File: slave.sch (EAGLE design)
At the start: 362 parts, among them J2 EB21A-06-D, J3 EB21A-06-D, J4 EB21A-06-D, J5 EB21A-06-D, J6 282837-9, J7 282837-9, J8 282837-9, J9 1715250000, Q1 DMN2056U-7, Q10 DMN2056U-7, Q11 DMN2056U-7, Q12 DMN2056U-7, Q13 DMN2056U-7, Q14 DMN2056U-7, Q15 DMN2056U-7, Q16 DMN2056U-7, Q17 DMN2056U-7, Q18 DMN2056U-7, Q19 DMN2056U-7, Q2 DMN2056U-7, Q20 DMN2056U-7, Q21 DMN2056U-7, Q22 DMN2056U-7, Q23 DMN2056U-7, Q24 DMN2056U-7, Q25 DMN2056U-7, Q26 DMN2056U-7, Q27 DMN2056U-7, Q28 DMN2056U-7, Q29 DMN2056U-7, Q3 DMN2056U-7, Q30 DMN2056U-7, Q31 DMN2056U-7, Q32 DMN2056U-7, Q33 DMN2056U-7, Q34 DMN2056U-7, Q35 DMN2056U-7, Q36 DMN2056U-7, Q37 DMN2056U-7, Q38 DMN2056U-7, Q39 DMN2056U-7, Q4 DMN2056U-7, Q40 DMN2056U-7, Q41 DMN2056U-7, Q42 DMN2056U-7, Q5 DMN2056U-7, Q7 DMN2056U-7, Q8 DMN2056U-7, Q9 DMN2056U-7, U1 INA332AIDGKR, U10 INA332AIDGKR, U11 INA332AIDGKR, U12 INA332AIDGKR, U13 INA332AIDGKR, U14 INA332AIDGKR, U15 INA332AIDGKR, U16 INA332AIDGKR, U17 INA332AIDGKR, U18 INA332AIDGKR, U19 INA332AIDGKR, U2 AP2112K-3.3TRG1, U20 INA332AIDGKR, U21 INA332AIDGKR, U22 INA332AIDGKR, U23 INA332AIDGKR, U24 INA332AIDGKR, U25 INA332AIDGKR, U26 INA332AIDGKR, U27 INA332AIDGKR, U28 INA332AIDGKR, U3 MCP23008-E/P, U4 MCP23008-E/P, U5 MCP23008-E/P, U6 MC74HCT4851ADR2G, U7 MC74HCT4851ADR2G, U8 MC74HCT4851ADR2G, U9 MC74HCT4851ADR2G

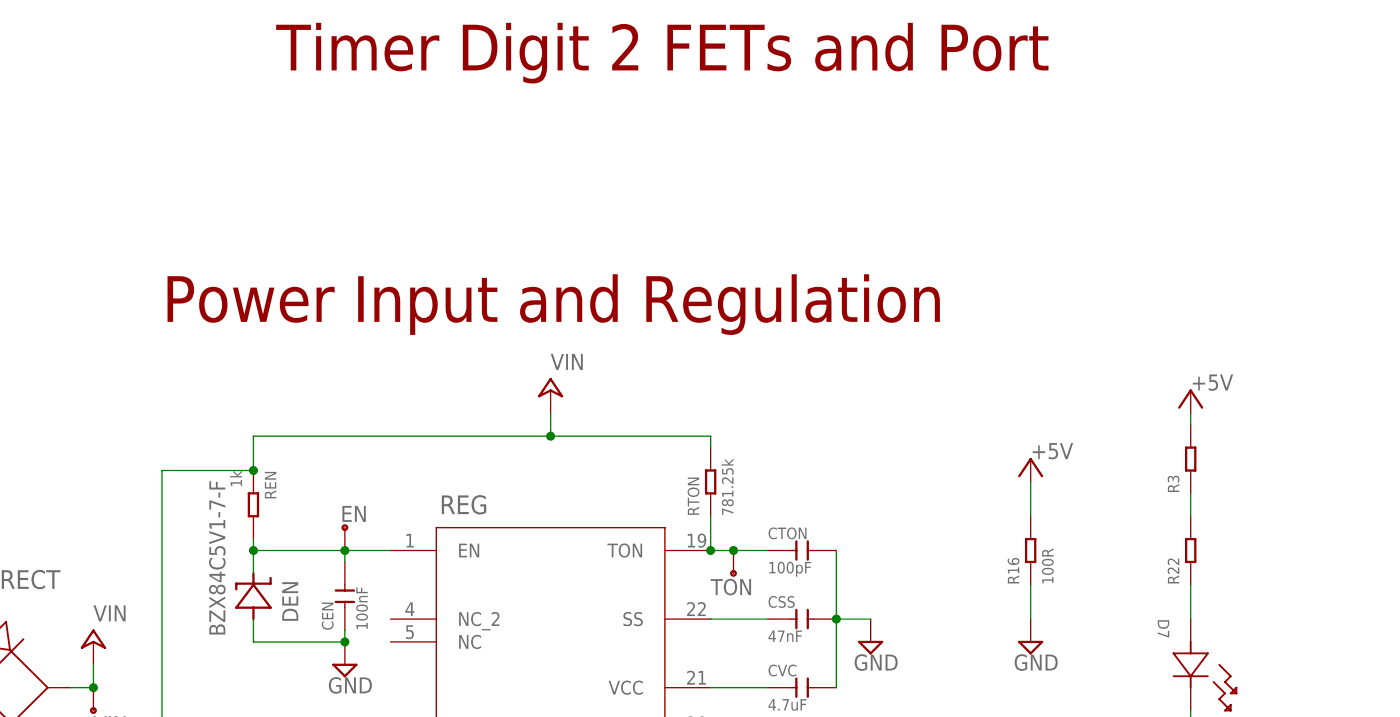
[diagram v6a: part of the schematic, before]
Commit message: updated RTON 781.25k resistor with series of 698k and 82.5k resistors, generated gerber and bom, cpl files
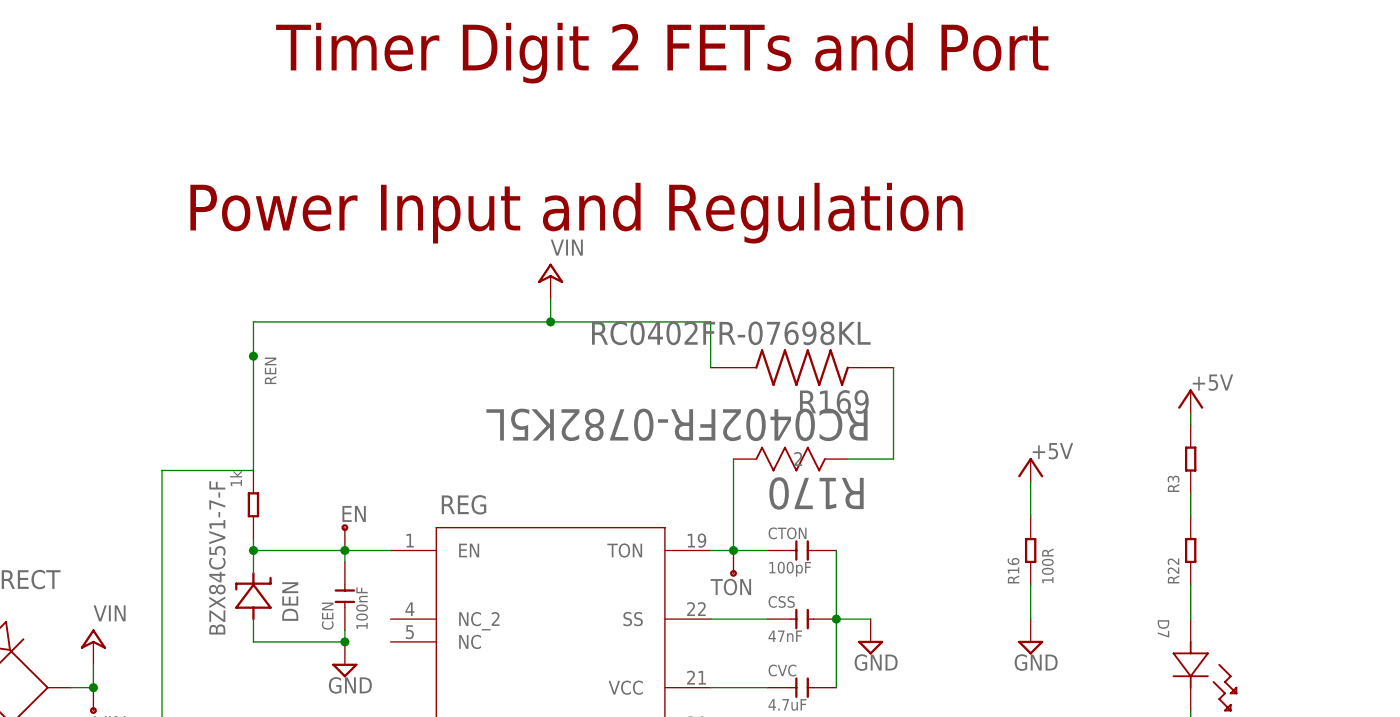
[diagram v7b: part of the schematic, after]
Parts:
- removed RTON: 781.25k, OPL_Resistor:SMD-RES-0R-1%-1/10W(0603)
- added R169: RC0402FR-07698KL, RC0402FR-07698KL:RC0402FR-07698KL
- added R170: RC0402FR-0782K5L, RC0402FR-0782K5L:RC0402FR-0782K5L
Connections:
- new net N$52: R169.1, R170.2
- net TON: now also R170.1; no longer RTON.1
- net VIN: now also R169.2; no longer RTON.2
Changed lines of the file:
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@@
 <layers>
 <layer number="1" name="Top" color="4" fill="1" visible="no" active="no"/>
-<layer number="2" name="Route2" color="21" fill="1" visible="no" active="no"/>
-<layer number="3" name="Route3" color="4" fill="3" visible="no" active="no"/>
-<layer number="4" name="Route4" color="1" fill="4" visible="no" active="no"/>
-<layer number="5" name="Route5" color="4" fill="4" visible="no" active="no"/>
-<layer number="6" name="Route6" color="1" fill="8" visible="no" active="no"/>
-<layer number="7" name="Route7" color="4" fill="8" visible="no" active="no"/>
-<layer number="8" name="Route8" color="1" fill="2" visible="no" active="no"/>
-<layer number="9" name="Route9" color="4" fill="2" visible="no" active="no"/>
-<layer number="10" name="Route10" color="1" fill="7" visible="no" active="no"/>
-<layer number="11" name="Route11" color="4" fill="7" visible="no" active="no"/>
-<layer number="12" name="Route12" color="1" fill="5" visible="no" active="no"/>
-<layer number="13" name="Route13" color="4" fill="5" visible="no" active="no"/>
-<layer number="14" name="Route14" color="1" fill="6" visible="no" active="no"/>
-<layer number="15" name="Route15" color="19" fill="1" visible="no" active="no"/>
+<layer number="2" name="Route2" color="16" fill="1" visible="no" active="no"/>
+<layer number="3" name="Route3" color="17" fill="1" visible="no" active="no"/>
+<layer number="4" name="Route4" color="18" fill="1" visible="no" active="no"/>
+<layer number="5" name="Route5" color="19" fill="1" visible="no" active="no"/>
+<layer number="6" name="Route6" color="25" fill="1" visible="no" active="no"/>
+<layer number="7" name="Route7" color="26" fill="1" visible="no" active="no"/>
+<layer number="8" name="Route8" color="27" fill="1" visible="no" active="no"/>
+<layer number="9" name="Route9" color="28" fill="1" visible="no" active="no"/>
+<layer number="10" name="Route10" color="29" fill="1" visible="no" active="no"/>
+<layer number="11" name="Route11" color="30" fill="1" visible="no" active="no"/>
+<layer number="12" name="Route12" color="20" fill="1" visible="no" active="no"/>
+<layer number="13" name="Route13" color="21" fill="1" visible="no" active="no"/>
+<layer number="14" name="Route14" color="22" fill="1" visible="no" active="no"/>
+<layer number="15" name="Route15" color="23" fill="1" visible="no" active="no"/>
 <layer number="16" name="Bottom" color="1" fill="1" visible="no" active="no"/>
 <layer number="17" name="Pads" color="2" fill="1" visible="no" active="no"/>
 <layer number="18" name="Vias" color="2" fill="1" visible="no" active="no"/>
 <layer number="19" name="Unrouted" color="6" fill="1" visible="no" active="no"/>
-<layer number="20" name="Dimension" color="15" fill="1" visible="no" active="no"/>
+<layer number="20" name="Dimension" color="24" fill="1" visible="no" active="no"/>
 <layer number="21" name="tPlace" color="7" fill="1" visible="no" active="no"/>
 <layer number="22" name="bPlace" color="7" fill="1" visible="no" active="no"/>
@@
 <part name="R1" library="OPL_Resistor" library_urn="urn:adsk.eagle:library:8004883" deviceset="SMD-RES-0R-1%-1/10W(0603)" device="" package3d_urn="urn:adsk.eagle:package:8004941/1" value="5.1k"/>
 <part name="R2" library="OPL_Resistor" library_urn="urn:adsk.eagle:library:8004883" deviceset="SMD-RES-0R-1%-1/10W(0603)" device="" package3d_urn="urn:adsk.eagle:package:8004941/1" value="27k"/>
-<part name="RTON" library="OPL_Resistor" library_urn="urn:adsk.eagle:library:8004883" deviceset="SMD-RES-0R-1%-1/10W(0603)" device="" package3d_urn="urn:adsk.eagle:package:8004941/1" value="781.25k"/>
 <part name="CSS" library="OPL_Capacitor" library_urn="urn:adsk.eagle:library:8004261" deviceset="CERAMIC-1NF-50V-10%-X7R(0603)" device="" package3d_urn="urn:adsk.eagle:package:8004287/1" value="47nF"/>
 <part name="CIN1" library="OPL_Capacitor" library_urn="urn:adsk.eagle:library:8004261" deviceset="CERAMIC-4.7UF-25V-10%-X5R(0805)" device="" package3d_urn="urn:adsk.eagle:package:8004286/1" value="10uF"/>
@@
 <part name="R168" library="RLC16-R100JTP - 100mOhm" deviceset="RLC16-R100JTP" device="" value="1m"/>
 <part name="SUPPLY37" library="supply2" library_urn="urn:adsk.eagle:library:372" deviceset="GND" device=""/>
+<part name="R169" library="RC0402FR-07698KL" deviceset="RC0402FR-07698KL" device=""/>
+<part name="R170" library="RC0402FR-0782K5L" deviceset="RC0402FR-0782K5L" device=""/>
 </parts>
 <sheets>
@@
 <plain>
 <frame x1="1270" y1="-635" x2="1955.8" y2="127" columns="8" rows="5" layer="94"/>
-<text x="1399.54" y="-469.9" size="5.08" layer="94">Power Input and Regulation</text>
+<text x="1402.08" y="-459.74" size="5.08" layer="94">Power Input and Regulation</text>
 <text x="1450.34" y="-591.82" size="5.08" layer="94" align="bottom-center">Power to ESP32
 (via 3V3 REG)</text>
@@
 <attribute name="VALUE" x="1485.9" y="-527.05" size="1.27" layer="96" ratio="10" rot="R270"/>
 </instance>
-<instance part="RTON" gate="G$1" x="1460.5" y="-487.68" smashed="yes" rot="R90">
-<attribute name="NAME" x="1459.23" y="-491.49" size="1.27" layer="95" ratio="10" rot="R90"/>
-<attribute name="VALUE" x="1463.04" y="-491.49" size="1.27" layer="96" ratio="10" rot="R90"/>
-</instance>
 <instance part="CSS" gate="G$1" x="1470.66" y="-502.92" smashed="yes">
 <attribute name="NAME" x="1466.85" y="-501.65" size="1.27" layer="95" ratio="10"/>
@@
 </instance>
 <instance part="REN" gate="G$1" x="1409.7" y="-490.22" smashed="yes" rot="R270">
-<attribute name="NAME" x="1410.97" y="-486.41" size="1.27" layer="95" ratio="10" rot="R270"/>
+<attribute name="NAME" x="1410.97" y="-473.71" size="1.27" layer="95" ratio="10" rot="R270"/>
 <attribute name="VALUE" x="1407.16" y="-486.41" size="1.27" layer="96" ratio="10" rot="R270"/>
 </instance>
@@
 <attribute name="VALUE" x="1406.5758" y="-504.8504" size="1.778" layer="96" rot="R90"/>
 </instance>
-<instance part="P+2" gate="1" x="1442.72" y="-477.52" smashed="yes">
-<attribute name="VALUE" x="1442.72" y="-475.234" size="1.778" layer="96"/>
+<instance part="P+2" gate="1" x="1442.72" y="-464.82" smashed="yes">
+<attribute name="VALUE" x="1442.72" y="-462.534" size="1.778" layer="96"/>
 </instance>
 <instance part="P+3" gate="1" x="1391.92" y="-505.46" smashed="yes">
@@
 <attribute name="VALUE" x="1826.895" y="-523.875" size="1.778" layer="96"/>
 </instance>
+<instance part="R169" gate="G$1" x="1470.66" y="-474.98" smashed="yes" rot="R180">
+<attribute name="NAME" x="1478.284440625" y="-477.52148125" size="2.54148125" layer="95" rot="R180"/>
+<attribute name="VALUE" x="1478.28996875" y="-469.893359375" size="2.54331875" layer="96" rot="R180"/>
+</instance>
+<instance part="R170" gate="A" x="1475.74" y="-485.14" smashed="yes" rot="R180">
+<attribute name="VALUE" x="1478.3562" y="-479.6028" size="3.4798" layer="96" ratio="10" rot="SR180"/>
+<attribute name="NAME" x="1477.9244" y="-487.2228" size="3.4798" layer="95" ratio="10" rot="SR180"/>
+</instance>
 </instances>
 <busses>
@@
 <segment>
 <pinref part="CTON" gate="G$1" pin="1"/>
-<pinref part="RTON" gate="G$1" pin="1"/>
 <wire x1="1460.5" y1="-495.3" x2="1463.04" y2="-495.3" width="0.1524" layer="91"/>
 <wire x1="1463.04" y1="-495.3" x2="1466.85" y2="-495.3" width="0.1524" layer="91"/>
-<wire x1="1460.5" y1="-495.3" x2="1460.5" y2="-491.49" width="0.1524" layer="91"/>
 <pinref part="REG" gate="A" pin="TON"/>
-<junction x="1460.5" y="-495.3"/>
 <pinref part="TON" gate="G$1" pin="1"/>
 <junction x="1463.04" y="-495.3"/>
+<pinref part="R170" gate="A" pin="1"/>
+<wire x1="1463.04" y1="-485.14" x2="1463.04" y2="-495.3" width="0.1524" layer="91"/>
 </segment>
 </net>
@@
 <wire x1="1399.54" y1="-486.41" x2="1399.54" y2="-519.43" width="0.1524" layer="91"/>
 <junction x="1399.54" y="-519.43"/>
-<wire x1="1409.7" y1="-486.41" x2="1409.7" y2="-482.6" width="0.1524" layer="91"/>
-<wire x1="1409.7" y1="-482.6" x2="1442.72" y2="-482.6" width="0.1524" layer="91"/>
-<junction x="1409.7" y="-486.41"/>
-<wire x1="1442.72" y1="-482.6" x2="1442.72" y2="-480.06" width="0.1524" layer="91"/>
-<pinref part="RTON" gate="G$1" pin="2"/>
-<wire x1="1442.72" y1="-482.6" x2="1460.5" y2="-482.6" width="0.1524" layer="91"/>
-<wire x1="1460.5" y1="-482.6" x2="1460.5" y2="-483.87" width="0.1524" layer="91"/>
-<junction x="1442.72" y="-482.6"/>
+<wire x1="1409.7" y1="-486.41" x2="1409.7" y2="-469.9" width="0.1524" layer="91"/>
+<wire x1="1409.7" y1="-469.9" x2="1442.72" y2="-469.9" width="0.1524" layer="91"/>
+<junction x="1409.7" y="-473.71"/>
+<wire x1="1442.72" y1="-469.9" x2="1442.72" y2="-467.36" width="0.1524" layer="91"/>
+<wire x1="1442.72" y1="-469.9" x2="1460.5" y2="-469.9" width="0.1524" layer="91"/>
+<wire x1="1460.5" y1="-469.9" x2="1460.5" y2="-471.17" width="0.1524" layer="91"/>
+<junction x="1442.72" y="-469.9"/>
 <pinref part="P+2" gate="1" pin="VIN"/>
+<pinref part="R169" gate="G$1" pin="2"/>
+<wire x1="1460.5" y1="-471.17" x2="1460.5" y2="-474.98" width="0.1524" layer="91"/>
 </segment>
 <segment>
@@
 </segment>
 </net>
+<net name="N$52" class="0">
+<segment>
+<pinref part="R169" gate="G$1" pin="1"/>
+<pinref part="R170" gate="A" pin="2"/>
+<wire x1="1480.82" y1="-474.98" x2="1480.82" y2="-485.14" width="0.1524" layer="91"/>
+<wire x1="1480.82" y1="-485.14" x2="1475.74" y2="-485.14" width="0.1524" layer="91"/>
+</segment>
+</net>
